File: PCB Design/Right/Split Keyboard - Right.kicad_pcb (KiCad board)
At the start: 2 copper layers, 258.4 x 134 mm, 121 parts, among them J1 AudioJack4, U1 ProMicroEliteC

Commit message: Added Left information. Tweaks to right side
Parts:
- D_A1, D_A10, D_A11, D_A2, D_A3, D_A4, D_A5, D_A6, D_A7, D_A8, D_A9, D_B1, D_B10, D_B11, D_B2, D_B3, D_B4, D_B5, D_B6, D_B7, D_B8, D_B9, D_C1, D_C10, D_C11, D_C12, D_C2, D_C3, D_C4, D_C5, D_C6, D_C7, D_C8, D_C9, D_D10, D_D11, D_D4, D_D5, D_D6, D_D7, D_D8, D_D9, D_E10, D_E11, D_E2, D_E4, D_E6, D_E7, D_E8, D_E9, D_F1, D_F2, D_F3, D_F4, D_F5, D_F6, D_F7, D_F8, D_F9: footprint Diode_THT:D_DO-35_SOD27_P3.81mm_Vertical_AnodeUp -> combodiode:ComboDiode
- moved SW_R1 3.40 mm to (110.1, 27.9)
- moved J1 3.00 mm to (198.1, 34.3)
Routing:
- net RowB: track 440.4 -> 489.8 mm
- net RowC: track 368.9 -> 323.1 mm
- net RowA: track 427.1 -> 385.1 mm
- net RowF: track 339.6 -> 311.6 mm
- net RowE: track 331.6 -> 306.0 mm
- net RowD: track 290.1 -> 272.9 mm
- net GND: track 358.3 -> 352.6 mm
- net VCC: track 202.9 -> 199.5 mm
- net Data2: track 188.9 -> 186.1 mm
- net Data1: track 192.4 -> 189.6 mm
- net Reset: track 289.7 -> 289.0 mm

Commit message: reworking PCB
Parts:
- J1: footprint Connector_Audio:Jack_3.5mm_PJ320D_Horizontal -> Keebio-Parts:TRRS-PJ-320A; moved to B.Cu
- SW_R1, U1: moved to B.Cu
- moved SW_R1 92.1 mm to (202.2, 31.2), turned to 180 degrees
- moved J1 84.7 mm to (113.5, 30.2), turned to 180 degrees
- moved U1 74.5 mm to (252.5, 43.9), turned to 270 degrees
- moved D_A1 14.7 mm to (253.0, 46.5), turned to 180 degrees
- moved D_A3 6.60 mm to (205.2, 42.2)
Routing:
- net RowB: track 489.8 -> 0.00 mm, vias 2 -> 0
- net RowA: track 385.1 -> 0.00 mm
- net GND: track 352.6 -> 0.00 mm
- net Col10: track 348.7 -> 0.00 mm
- net Col9: track 344.3 -> 0.00 mm
- net Col11: track 340.7 -> 0.00 mm
- net RowC: track 323.1 -> 0.00 mm, vias 2 -> 0
- net RowF: track 311.6 -> 0.00 mm, vias 2 -> 0
- net RowE: track 306.0 -> 0.00 mm
- net Col8: track 290.7 -> 0.00 mm
- net Col12: track 289.8 -> 0.00 mm
- net Reset: track 289.0 -> 0.00 mm
- net RowD: track 272.9 -> 0.00 mm
- net Col7: track 271.6 -> 0.00 mm
- net Col6: track 249.9 -> 0.00 mm
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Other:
- board outline removed

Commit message: Updated Right PCB
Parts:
- moved D_D5 6.69 mm to (133.1, 108.5)
- moved D_D6 6.69 mm to (114.0, 108.5)
- moved D_D7 6.69 mm to (95.0, 108.5)
- moved D_D8 6.69 mm to (75.9, 108.5)
- moved D_D10 6.64 mm to (37.7, 108.5)
- moved D_D11 6.64 mm to (18.7, 108.5)
- moved D_D4 6.64 mm to (152.2, 108.5)
- moved D_D9 6.64 mm to (56.8, 108.5)
- moved D_C12 6.54 mm to (13.9, 89.4)
- moved D_E10 6.54 mm to (47.3, 127.5)
- moved D_E11 6.54 mm to (28.2, 127.5)
- moved D_E4 6.54 mm to (142.6, 127.5)
- moved D_E6 6.54 mm to (123.5, 127.5)
- moved D_E7 6.54 mm to (104.5, 127.5)
- moved D_E8 6.54 mm to (85.4, 127.5)
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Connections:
- U1 pad 10: RowD -> Col11
- U1 pad 11: RowE -> Col1
- U1 pad 12: RowF -> Col10
- U1 pad 13: Col8 -> RowF
- U1 pad 14: Col9 -> RowE
- U1 pad 15: Col10 -> RowD
- U1 pad 16: Col11 -> RowC
- U1 pad 17: Col12 -> RowB
- U1 pad 18: Col1 -> RowA
- U1 pad 19: Col2 -> Col3
- U1 pad 20: Col3 -> Col2
- U1 pad 25: Net-(U1-Pad25) -> Col9
- U1 pad 26: Col4 -> Col8
- U1 pad 27: Col5 -> Col7
- U1 pad 29: Col7 -> Col5
- U1 pad 7: RowC -> Net-(U1-Pad7)
- U1 pad 8: RowA -> Col4
- U1 pad 9: RowB -> Col12
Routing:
- net RowF: track 0.00 -> 366.0 mm
- net Col11: track 0.00 -> 339.2 mm, vias 0 -> 3
- net RowE: track 0.00 -> 336.5 mm, vias 0 -> 2
- net Col9: track 0.00 -> 326.3 mm, vias 0 -> 3
- net RowC: track 0.00 -> 324.1 mm, vias 0 -> 1
- net Col10: track 0.00 -> 310.9 mm, vias 0 -> 3
- net RowB: track 0.00 -> 296.5 mm, vias 0 -> 1
- net Col8: track 0.00 -> 288.2 mm, vias 0 -> 3
- net RowD: track 0.00 -> 286.2 mm
- net Col12: track 0.00 -> 281.2 mm, vias 0 -> 4
- net Col7: track 0.00 -> 267.5 mm, vias 0 -> 3
- net Col6: track 0.00 -> 245.1 mm, vias 0 -> 3
- net Col5: track 0.00 -> 228.8 mm, vias 0 -> 3
- net RowA: track 0.00 -> 225.7 mm
- net Col4: track 0.00 -> 209.1 mm, vias 0 -> 1
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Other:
- board outline added: 252.1 x 129.5 mm

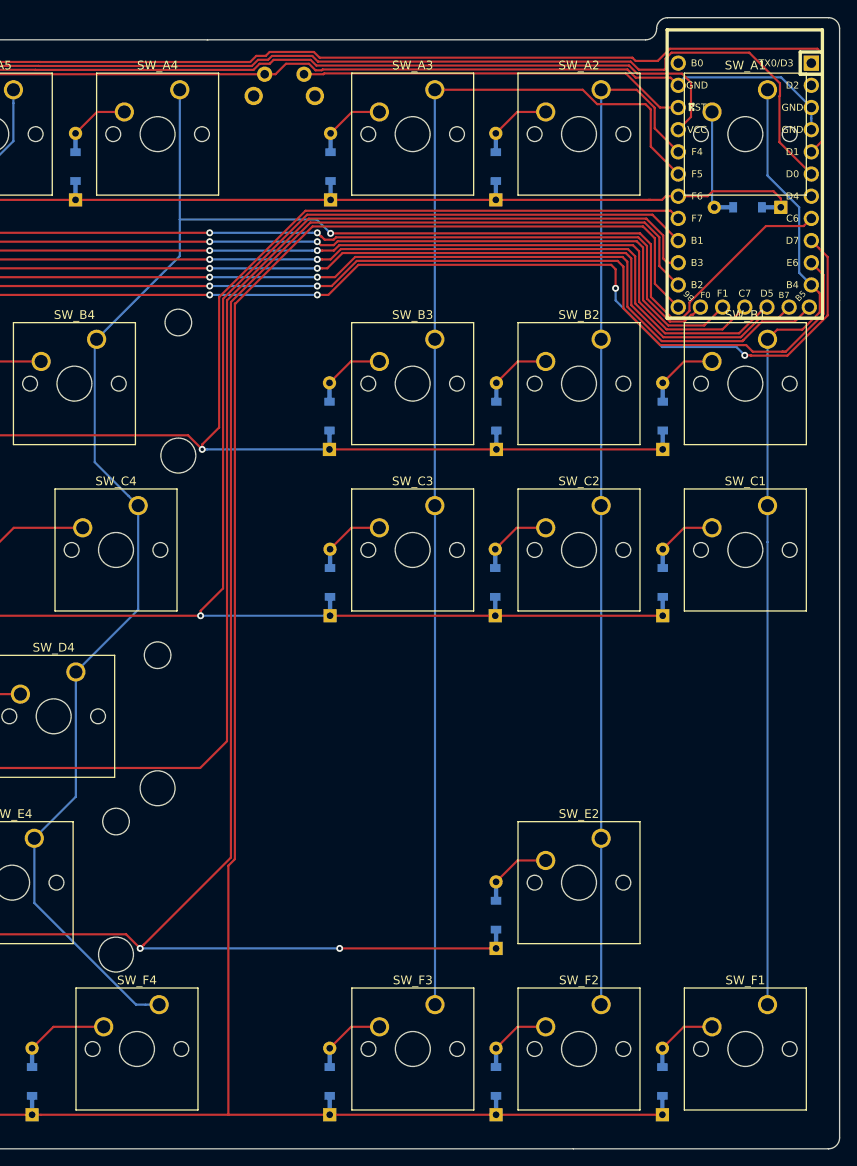
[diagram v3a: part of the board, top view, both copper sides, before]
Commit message: Finished PCBs, added DXF and Gerber files
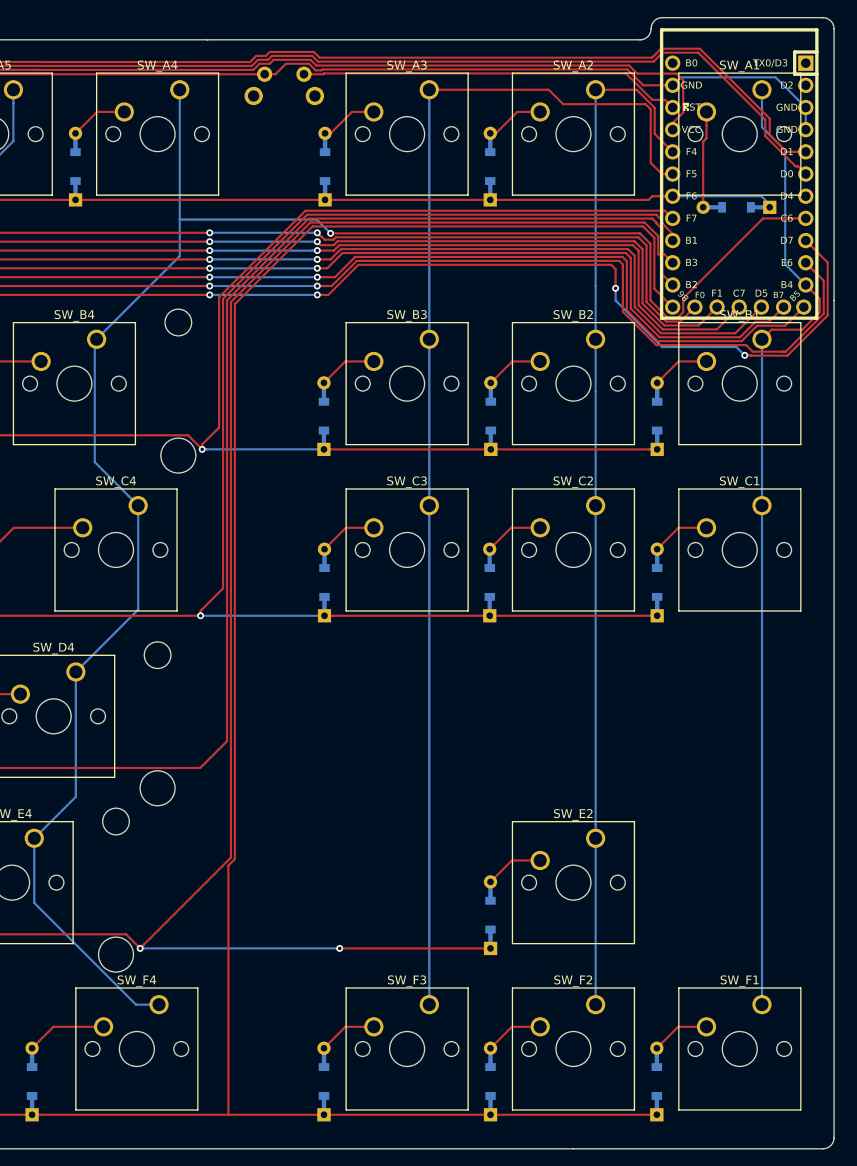
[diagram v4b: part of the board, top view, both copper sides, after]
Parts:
- moved D_A1 1.27 mm to (251.7, 46.5)
- moved D_F3 0.65 mm to (204.5, 146.6)
- moved SW_F3 0.65 mm to (216.5, 137.8)
- moved D_B2 0.64 mm to (223.6, 70.4)
- moved SW_A1 0.64 mm to (254.6, 33.0)
- moved SW_B1 0.64 mm to (254.6, 61.6)
- moved SW_C1 0.64 mm to (254.6, 80.6)
- moved SW_F1 0.64 mm to (254.6, 137.8)
- moved U1 0.64 mm to (252.0, 43.9)
- moved D_A2 0.63 mm to (223.5, 41.8)
- moved D_A3 0.63 mm to (204.6, 41.8)
- moved D_B1 0.63 mm to (242.6, 70.4)
- moved D_B3 0.63 mm to (204.5, 70.4)
- moved D_C1 0.63 mm to (242.6, 89.4)
- moved D_C2 0.63 mm to (223.5, 89.4)
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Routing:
- net Data2: track 165.5 -> 157.2 mm
- net Data1: track 165.6 -> 160.6 mm
- net RowA: track 225.7 -> 223.3 mm
- net RowB: track 296.5 -> 295.2 mm
- net Col3: track 139.1 -> 140.3 mm
- net Col1: track 111.4 -> 112.4 mm
- net RowF: track 366.0 -> 365.1 mm
- net RowE: track 336.5 -> 335.6 mm
- net VCC: track 149.7 -> 148.8 mm
- net GND: track 159.6 -> 158.8 mm
- net RowD: track 286.2 -> 286.9 mm
- net RowC: track 324.1 -> 323.4 mm
- net Col11: track 339.2 -> 339.8 mm
- net Reset: track 44.5 -> 43.9 mm
- net Col5: track 228.8 -> 229.4 mm
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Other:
- board size 252.1 x 129.5 mm -> 251.5 x 129.5 mm
